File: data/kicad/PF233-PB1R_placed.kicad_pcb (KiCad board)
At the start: 4 copper layers, 70 x 70 mm, 39 parts, among them M12 12 V 1.5 A switching module, Q1A 650V SJ 95mR, Q1B 650V SJ 95mR, U1 TC4420, U3 LM393

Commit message: Step 3: PB1R routed (rectangular board), KiCad 9 clean, KiCad-written Gerbers with plane read-back, cross-check vs the TX stage
- router.py / drc.py rectangular outline; pads.json for PB1R; route_run PB1R (hatched GND/VBUS planes, DRAIN1/CLAMP1 HV 1.0 mm); rect_inject.py; kicad_gerber.py (zones filled with the HV rules, kicad-cli Gerbers and drill)
- cross-check (pb1r_check.py) drove a re-placement: JL1 to the left edge (DRAIN1 15/33 mm, 4.9 mohm), Kelvin sense ECO (route_fix), via farm (viafarm.py), narrow GND/VBUS stubs
- results: route 15 nets 0 failures; independent DRC 0/0; KiCad 9 0 errors / 0 unconnected with the HV negative control; plane Gerbers >= 1.000 mm from HV pads/vias (gerbonara + shapely read-back, control passed)
- neck-module eddy: solid plane would return 8x a 1 g nugget at 150 mm (rejected); hatched border ring 4.7e-5
- regress 47 pass; make route-pb1r / drc-pb1r / kicad-pb1r / gerber-pb1r / check-pb1r; requirements-cam.txt
- CORRECTIONS, DESIGN_STATE, OPEN_ITEMS 28, ASSUMPTIONS 32, FAB_RULES (via-in-pad)

Not done: Steps 4-6 (PM2/HB2 routing, datasheets and vendor sheets, bench procedure); no CAM viewer; nothing built or measured.

Co-Authored-By: Claude Sonnet 5.5 <noreply@anthropic.com>
Claude-Session: https://claude.ai/code/session_01T7iU5pGiBfkKRBbe2JcTJx
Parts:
- moved JL1 62.0 mm to (69.0, 80.0)
- moved CK1 14.9 mm to (96.0, 107.0)
- moved RK1 14.9 mm to (92.0, 107.0)
- moved CU3 10.0 mm to (110.0, 110.0)
- moved U3 10.0 mm to (104.0, 110.0)
- moved DC1 1.50 mm to (70.5, 89.5)
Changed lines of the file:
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@@
     (0 "F.Cu" signal) (1 "In1.Cu" signal) (2 "In2.Cu" signal) (31 "B.Cu" signal) (34 "B.Paste" user) (35 "F.Paste" user) (36 "B.SilkS" user "B.Silkscreen") (37 "F.SilkS" user "F.Silkscreen")
     (38 "B.Mask" user) (39 "F.Mask" user) (40 "Dwgs.User" user "User.Drawings") (41 "Cmts.User" user "User.Comments") (44 "Edge.Cuts" user) (47 "F.CrtYd" user "F.Courtyard") (49 "F.Fab" user))
-  (setup (pad_to_mask_clearance 0.05) (stackup (layer "F.Cu" (type "copper") (thickness 0.07)) (layer "dielectric 1" (type "prepreg") (thickness 0.2)) (layer "In1.Cu" (type "copper") (thickness 0.035)) (layer "dielectric 2" (type "core") (thickness 1.0)) (layer "In2.Cu" (type "copper") (thickness 0.035)) (layer "dielectric 3" (type "prepreg") (thickness 0.2)) (layer "B.Cu" (type "copper") (thickness 0.07)) (copper_finish "ENIG")))
+  (setup (pad_to_mask_clearance 0.05) (stackup (layer "F.Cu" (type "copper") (thickness 0.07)) (layer "dielectric 1" (type "prepreg") (thickness 0.2)) (layer "In1.Cu" (type "copper") (thickness 0.035)) (layer "dielectric 2" (type "core") (thickness 1.0)) (layer "In2.Cu" (type "copper") (thickness 0.035)) (layer "dielectric 3" (type "prepreg") (thickness 0.2)) (layer "B.Cu" (type "copper") (thickness 0.07)) (copper_finish "HASL lead-free")))
   (net 0 "")
   (net 1 "AUX12")
@@
     (pad "2" smd roundrect (at 0.825 0.000) (size 0.800 0.950) (layers "F.Cu" "F.Paste" "F.Mask") (net 10 "GND"))
   )
-  (footprint "Package_SO:SOIC-8_3.9x4.9mm_P1.27mm" (layer "F.Cu") (at 114.0000 110.0000)
+  (footprint "Package_SO:SOIC-8_3.9x4.9mm_P1.27mm" (layer "F.Cu") (at 104.0000 110.0000)
     (property "Reference" "U3" (at 0 -2.5 0) (layer "F.SilkS") (effects (font (size 0.8 0.8) (thickness 0.12))))
     (property "Value" "LM393" (at 0 2.5 0) (layer "F.Fab") (effects (font (size 0.8 0.8) (thickness 0.12))))
@@
     (pad "8" smd roundrect (at 2.700 -1.905) (size 1.550 0.600) (layers "F.Cu" "F.Paste" "F.Mask") (net 1 "AUX12"))
   )
-  (footprint "Capacitor_SMD:C_0805_2012Metric" (layer "F.Cu") (at 120.0000 110.0000)
+  (footprint "Capacitor_SMD:C_0805_2012Metric" (layer "F.Cu") (at 110.0000 110.0000)
     (property "Reference" "CU3" (at 0 -2.5 0) (layer "F.SilkS") (effects (font (size 0.8 0.8) (thickness 0.12))))
     (property "Value" "1u 25V" (at 0 2.5 0) (layer "F.Fab") (effects (font (size 0.8 0.8) (thickness 0.12))))
@@
     (pad "2" smd roundrect (at 3.100 0.000) (size 1.600 3.400) (layers "F.Cu" "F.Paste" "F.Mask") (net 10 "GND"))
   )
-  (footprint "Diode_SMD:D_SMC" (layer "F.Cu") (at 70.5000 88.0000)
+  (footprint "Diode_SMD:D_SMC" (layer "F.Cu") (at 70.5000 89.5000)
     (property "Reference" "DC1" (at 0 -2.5 0) (layer "F.SilkS") (effects (font (size 0.8 0.8) (thickness 0.12))))
     (property "Value" "ES3J 600V 3A" (at 0 2.5 0) (layer "F.Fab") (effects (font (size 0.8 0.8) (thickness 0.12))))
@@
     (pad "2" thru_hole circle (at 2.540 0.000) (size 3.0 3.0) (drill 1.6) (layers "*.Cu" "*.Mask") (net 19 "VBUS"))
   )
-  (footprint "Connector:Terminal_block_1x2_P5.08mm" (layer "F.Cu") (at 131.0000 80.0000)
+  (footprint "Connector:Terminal_block_1x2_P5.08mm" (layer "F.Cu") (at 69.0000 80.0000)
     (property "Reference" "JL1" (at 0 -2.5 0) (layer "F.SilkS") (effects (font (size 0.8 0.8) (thickness 0.12))))
     (property "Value" "Coil outer band: DRAIN, VBUS" (at 0 2.5 0) (layer "F.Fab") (effects (font (size 0.8 0.8) (thickness 0.12))))
@@
     (pad "2" thru_hole circle (at 0.000 2.540) (size 3.0 3.0) (drill 1.7) (layers "*.Cu" "*.Mask") (net 19 "VBUS"))
   )
-  (footprint "Resistor_SMD:R_0603_1608Metric" (layer "F.Cu") (at 106.0000 102.0000)
+  (footprint "Resistor_SMD:R_0603_1608Metric" (layer "F.Cu") (at 92.0000 107.0000)
     (property "Reference" "RK1" (at 0 -2.5 0) (layer "F.SilkS") (effects (font (size 0.8 0.8) (thickness 0.12))))
     (property "Value" "100" (at 0 2.5 0) (layer "F.Fab") (effects (font (size 0.8 0.8) (thickness 0.12))))
@@
     (pad "2" smd roundrect (at 0.825 0.000) (size 0.800 0.950) (layers "F.Cu" "F.Paste" "F.Mask") (net 11 "ISENSE1"))
   )
-  (footprint "Capacitor_SMD:C_0603_1608Metric" (layer "F.Cu") (at 110.0000 102.0000)
+  (footprint "Capacitor_SMD:C_0603_1608Metric" (layer "F.Cu") (at 96.0000 107.0000)
     (property "Reference" "CK1" (at 0 -2.5 0) (layer "F.SilkS") (effects (font (size 0.8 0.8) (thickness 0.12))))
     (property "Value" "100p" (at 0 2.5 0) (layer "F.Fab") (effects (font (size 0.8 0.8) (thickness 0.12))))

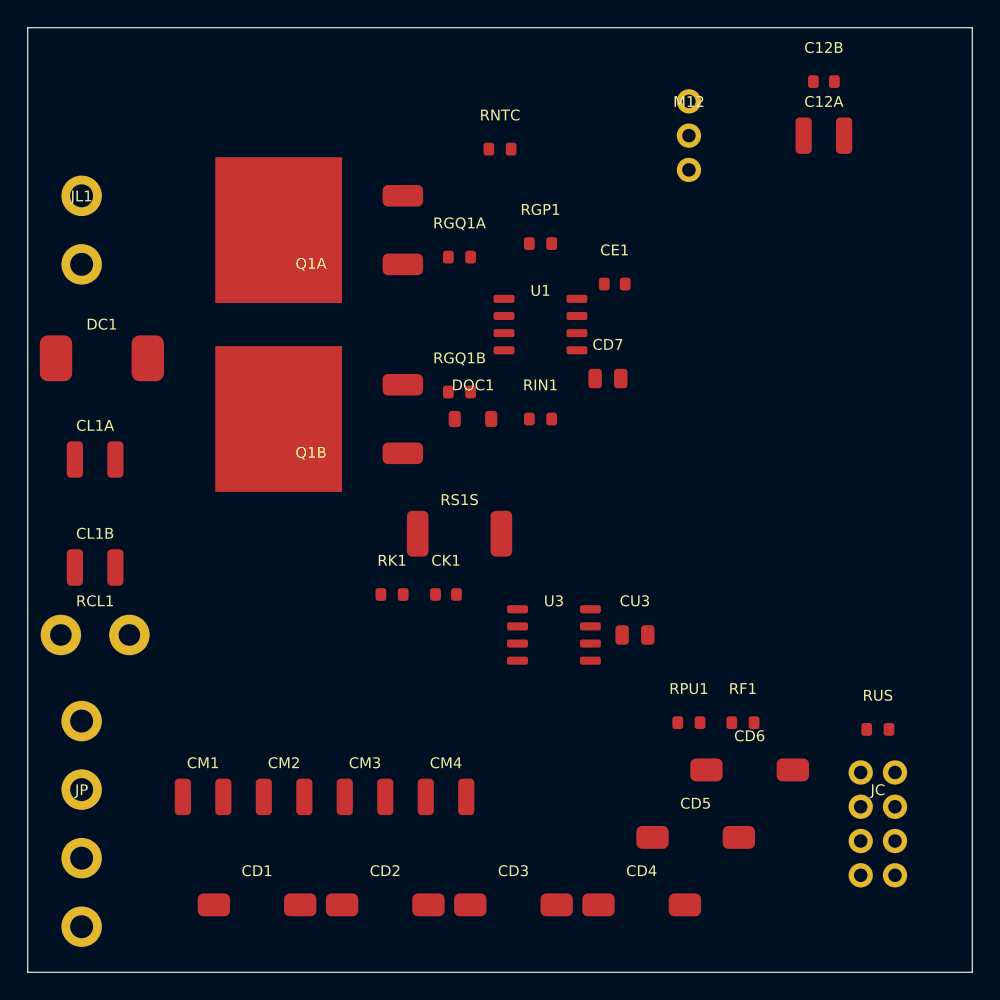
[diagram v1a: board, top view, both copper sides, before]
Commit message: Step 5: datasheets and fabricator sheets (vendor-derived floor, verified parts, PB1R 9-can bank, Gerber edge read-back)
- Fab floor from AdvancedPCB / TTM pages (docs/design/FAB_RULES_VERIFIED.md, U-FAB-RULES closed): clearance 0.16,
  component-PTH ring 0.18 / hole 0.46, drill-copper 0.26, drill-drill 0.41, every rule (severity error).
  CB1D JA/JB and HB2 TO-92 pads 1.02 mm; route_fix merges close same-net vias (CB1D, LB1).
- Parts from manufacturer PDFs (docs/design/DATASHEET_LOG.md): PB1R bulk 9 x Panasonic EEHZC1H101P
  (the 150 uF / 50 V polymer-Ta was not found; bank stays 900 uF, on-time table unchanged), PB1R re-placed
  with the Kelvin/comparator cluster pinned (pulse path 4.9 mohm, spike 7.5 V, ground ref 15.5 mV unchanged);
  SMCJ30A (SMCJ33A clamps 53.3 V > 50 V parts), Si4401FDY, BZT52C15, Bourns SF-1206S500-2 (new 1206 land),
  DRV5023BIQLPG, CRCW2512 500 V, OPA2365/OPA2211/LM393/CD74HC4051 checked. ES3J 600 V kept as a WATCH.
- U-DS-PARTS split into groups; open: TXDRIVE, OKI, PACK, BAV199, HVTERM. U-COLD-BOOTSTRAP closed.
- Controls retargeted to fixture folders (12/12). Netlist date fixed (data changed daily).
- Gerber planes from gerber_out.py ran into the notch and to 0.1 mm of the edge since r1 (found by the
  independent review): fixed, and gerber_edge_check.py reads every copper layer back.
- New Gerber sets CB1D_B3, LB1_v5, PB1R_v2; old sets marked SUPERSEDED.
- Findings for the owner: aluminium cans ~0.5 x a 1 g nugget (OPEN_ITEMS 34), OPA2365 capacitive load (30),
  OPA2211 input range on 5 V (31), Hall magnet spread (32).
- Strict regress 55 PASS / 0 FAIL / 0 SKIP; sign-off 44 PASS / 0 FAIL / 0 SKIP / 19 UNVERIFIED.

Co-Authored-By: Claude Opus 5.5 <noreply@anthropic.com>
Claude-Session: https://claude.ai/code/session_015VKhZtgEAWnezB2NDY75VV
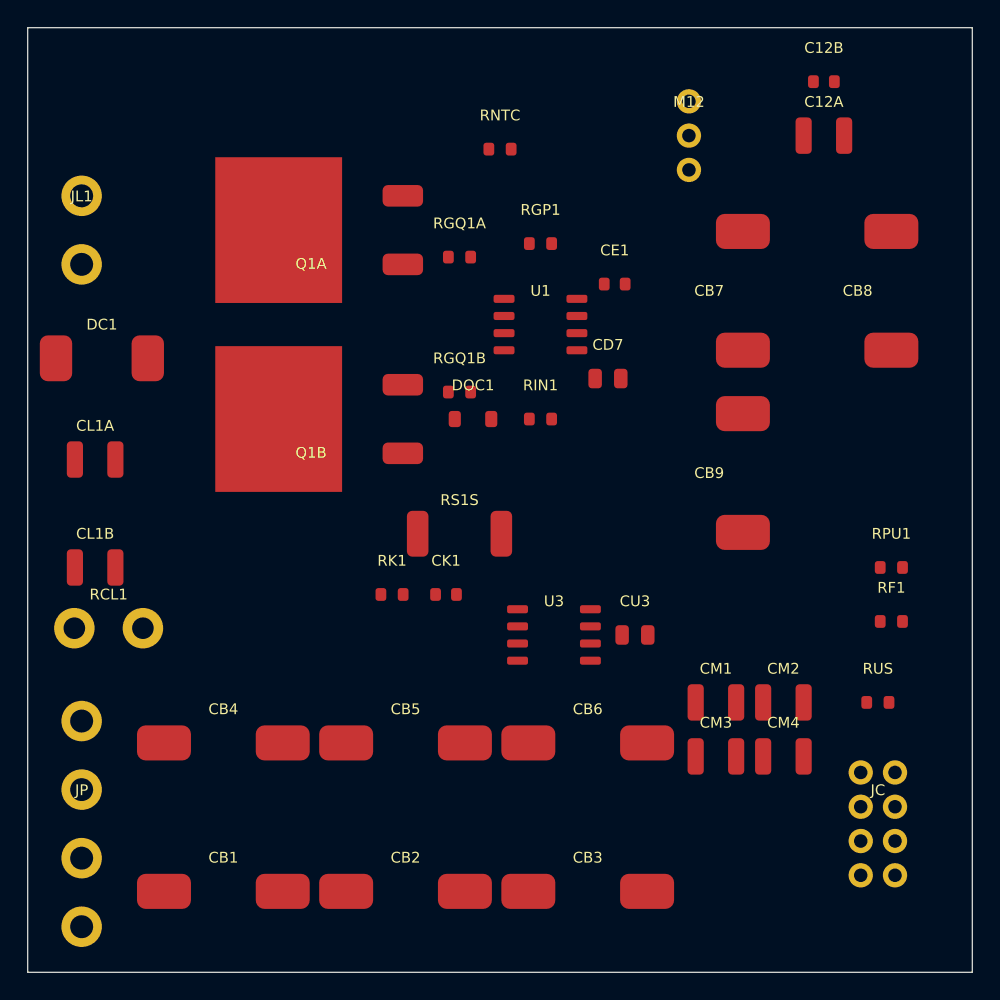
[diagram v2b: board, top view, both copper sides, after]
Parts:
- removed CD1, CD2, CD3, CD4, CD5, CD6: 150u 50V polymer Ta, Capacitor_Tantalum_SMD:CP_EIA-7343-43_Kemet-X
- added CB1: 100u 50V hybrid, Capacitor_SMD:CP_Elec_10x10, F.Cu at (79.5, 129.0)
- added CB2: 100u 50V hybrid, Capacitor_SMD:CP_Elec_10x10, F.Cu at (93.0, 129.0)
- added CB3: 100u 50V hybrid, Capacitor_SMD:CP_Elec_10x10, F.Cu at (106.5, 129.0)
- added CB4: 100u 50V hybrid, Capacitor_SMD:CP_Elec_10x10, F.Cu at (79.5, 118.0)
- added CB5: 100u 50V hybrid, Capacitor_SMD:CP_Elec_10x10, F.Cu at (93.0, 118.0)
- added CB6: 100u 50V hybrid, Capacitor_SMD:CP_Elec_10x10, F.Cu at (106.5, 118.0)
- added CB7: 100u 50V hybrid, Capacitor_SMD:CP_Elec_10x10, F.Cu at (118.0, 84.5)
- added CB8: 100u 50V hybrid, Capacitor_SMD:CP_Elec_10x10, F.Cu at (129.0, 84.5)
- added CB9: 100u 50V hybrid, Capacitor_SMD:CP_Elec_10x10, F.Cu at (118.0, 98.0)
- RS1S: value 10m 3W -> 10m 1W
- moved CM1 38.6 mm to (116.0, 115.0)
- moved CM2 37.7 mm to (121.0, 115.0)
- moved CM3 26.2 mm to (116.0, 119.0)
- moved CM4 25.2 mm to (121.0, 119.0)
- moved RPU1 18.9 mm to (129.0, 105.0)
- moved RF1 13.3 mm to (129.0, 109.0)
- moved RUS 2.00 mm to (128.0, 115.0)
- moved RCL1 1.12 mm to (71.0, 109.5)

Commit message: WIP checkpoint (audit): PB1R/NPM fit fixed (NPM body v2 rails, dam v2, PB1R_v3), fit check and guards; source+data
Co-Authored-By: Claude Sonnet 5.5 <noreply@anthropic.com>
Claude-Session: https://claude.ai/code/session_015VKhZtgEAWnezB2NDY75VV
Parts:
- moved CB8 13.5 mm to (128.5, 98.0)
- moved CB6 13.0 mm to (118.0, 112.0)
- moved CB5 12.3 mm to (87.5, 107.0)
- moved CB3 11.2 mm to (104.5, 118.0)
- moved CB2 11.0 mm to (104.0, 129.0)
- moved RK1 6.50 mm to (98.5, 106.8)
- moved CM1 4.53 mm to (116.5, 119.5)
- moved CM2 4.53 mm to (121.5, 119.5)
- moved RS1S 4.50 mm to (101.5, 102.5)
- moved CM3 4.03 mm to (116.5, 123.0)
- moved CM4 4.03 mm to (121.5, 123.0)
- moved CK1 3.75 mm to (98.5, 109.8)
- moved DOC1 1.50 mm to (99.5, 94.0)
- moved RGQ1A 1.50 mm to (98.5, 82.0)
- moved RGQ1B 1.50 mm to (98.5, 92.0)
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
